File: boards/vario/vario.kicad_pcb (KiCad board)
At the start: 2 copper layers, 90 x 100 mm, 121 parts, among them J1 Conn_02x20_Odd_Even, J2 SD_Card, J3 Mini-DIN-6, Q1 2N7002, Q2 2N7002, Q3 2N7002, Q4 2N7002, Q5 2N7002, U1 74HC273PW, U10 74HC161PW, U11 MC74HC244ADT, U12 74HC74PW, U13 74HC74PW, U14 74HC08PW, U15 74HC74PW, U16 74HC74PW, U17 74HC161PW, U18 74HC273PW, U19 CD74HC280MT, U2 74HC161PW, U20 MC74HC151ADTR2G, U21 MC74HC151ADTR2G, U22 MC74HC244ADT, U23 CD74HC280MT, U24 SN74LV10APW, U25 74HC08PW, U26 74HC04PW, U27 74HC30D, U28 SN74HC32PWR, U29 SN74HC32PWR, U3 74HC74PW, U30 SN74HC32PWR, U31 SN74LV14APW, U32 SN74HC32PWR, U33 74HC08PW, U34 74HC273PW, U35 MC74HC244ADT, U36 IFX54441EJV33, U37 SN74HC139PW, U38 SN74HC32PWR, U4 74HC273PW, U5 MC74HC151ADTR2G, U6 MC74HC244ADT, U7 SN74LV14APW, U8 74HC273PW, U9 74HC273PW

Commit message: Vario: power nets
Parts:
- moved R5 214.2 mm to (129.5, 83.2), turned to 90 degrees
- moved C29 203.4 mm to (139.2, 70.0), turned to 180 degrees
- moved C33 201.7 mm to (132.8, 81.2), turned to 90 degrees
- moved Q2 200.9 mm to (130.5, 92.0)
- moved C34 200.8 mm to (138.8, 82.2), turned to 180 degrees
- moved C31 195.5 mm to (152.5, 73.2)
- moved U32 195.4 mm to (135.8, 63.5)
- moved D2 194.8 mm to (142.8, 52.5), turned to 180 degrees
- moved C36 194.3 mm to (152.5, 59.0)
- moved U33 191.4 mm to (149.0, 63.0)
- moved R19 191.3 mm to (146.4, 52.5), turned to 180 degrees
- moved C35 189.5 mm to (139.2, 59.5), turned to 180 degrees
- moved U3 188.5 mm to (135.8, 74.0)
- moved U31 188.4 mm to (135.5, 86.2)
- moved C28 185.8 mm to (153.8, 83.2)
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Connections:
- U1 pad 12: /SPI/reg_send_q4 -> /SPI/reg_send_q0
- U1 pad 13: /d4 -> /d0
- U1 pad 14: /d5 -> /d1
- U1 pad 15: /SPI/reg_send_q5 -> /SPI/reg_send_q1
- U1 pad 16: /SPI/reg_send_q6 -> /SPI/reg_send_q2
- U1 pad 17: /d6 -> /d2
- U1 pad 18: /d7 -> /d3
- U1 pad 19: /SPI/reg_send_q7 -> /SPI/reg_send_q3
- U1 pad 2: /SPI/reg_send_q0 -> /SPI/reg_send_q4
- U1 pad 3: /d0 -> /d4
- U1 pad 4: /d1 -> /d5
- U1 pad 5: /SPI/reg_send_q1 -> /SPI/reg_send_q5
- U1 pad 6: /SPI/reg_send_q2 -> /SPI/reg_send_q6
- U1 pad 7: /d2 -> /d6
- U1 pad 8: /d3 -> /d7
- U1 pad 9: /SPI/reg_send_q3 -> /SPI/reg_send_q7
- U13 pad 11: /ps2/send_clk_ena_clk -> /ps2/send_req
- U13 pad 13: /ps2/~send_rst -> /ps2/~send_clk_out_rst
- U13 pad 8: /ps2/~send_clk_ena -> /ps2/send_clk_out
- U13 pad 9: (no net) -> /ps2/~send_clk_out
- U15 pad 1: /ps2/~send_clk_out_rst -> /ps2/~send_rst
- U15 pad 3: /ps2/send_req -> /ps2/send_clk_ena_clk
- U15 pad 5: /ps2/~send_clk_out -> (no net)
- U15 pad 6: /ps2/send_clk_out -> /ps2/~send_clk_ena
- U18 pad 12: /ps2/send_data5 -> /ps2/send_data1
- U18 pad 13: /d4 -> /d0
- U18 pad 14: /d5 -> /d1
- U18 pad 15: /ps2/send_data6 -> /ps2/send_data2
- U18 pad 16: /ps2/send_data7 -> /ps2/send_data3
- U18 pad 17: /d6 -> /d2
- U18 pad 18: /d7 -> /d3
- U18 pad 19: /ps2/send_data8 -> /ps2/send_data4
- U18 pad 2: /ps2/send_data1 -> /ps2/send_data5
- U18 pad 3: /d0 -> /d4
- U18 pad 4: /d1 -> /d5
- U18 pad 5: /ps2/send_data2 -> /ps2/send_data6
- U18 pad 6: /ps2/send_data3 -> /ps2/send_data7
- U18 pad 7: /d2 -> /d6
- U18 pad 8: /d3 -> /d7
- U18 pad 9: /ps2/send_data4 -> /ps2/send_data8
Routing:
- net GND: track 0.00 -> 1167.6 mm, vias 0 -> 90
- net VCC: track 0.00 -> 609.3 mm, vias 0 -> 45
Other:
- rule trace_min: 0.2 -> 0.1524

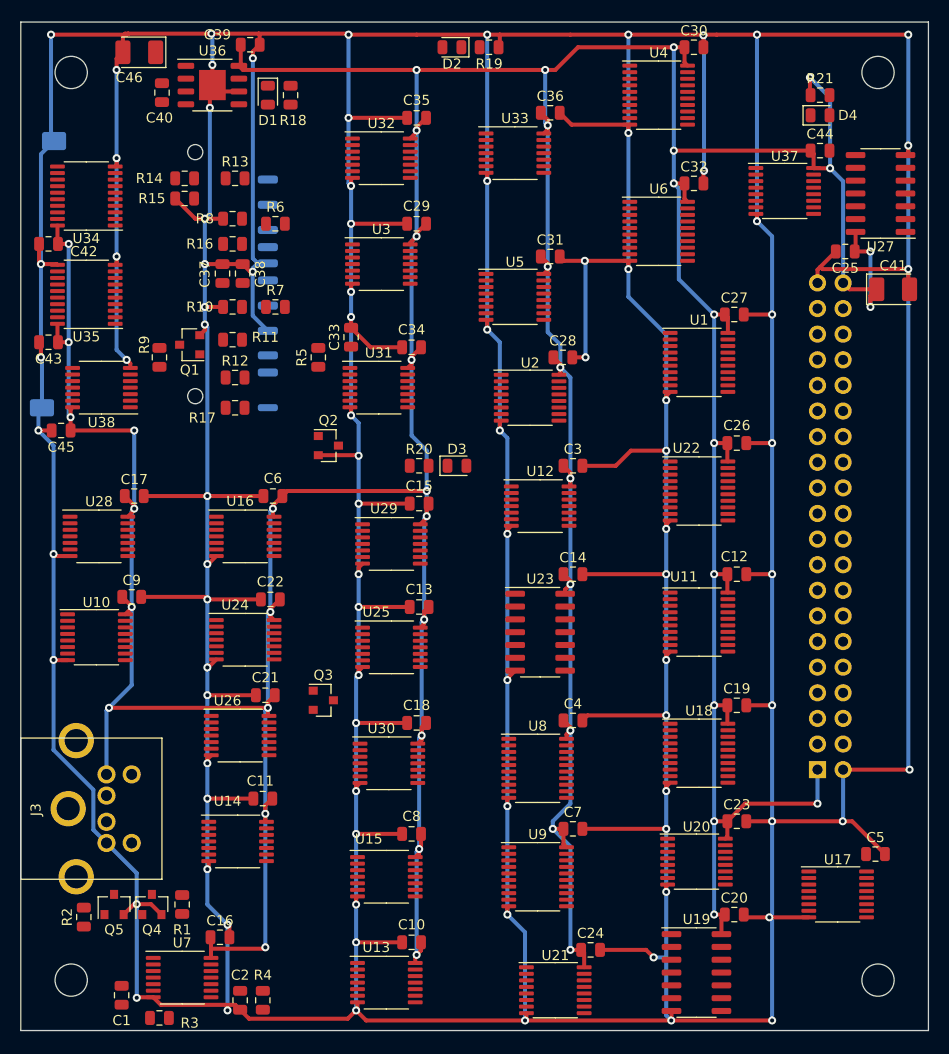
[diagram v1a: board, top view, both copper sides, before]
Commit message: Vario: board, delete redundant 7474
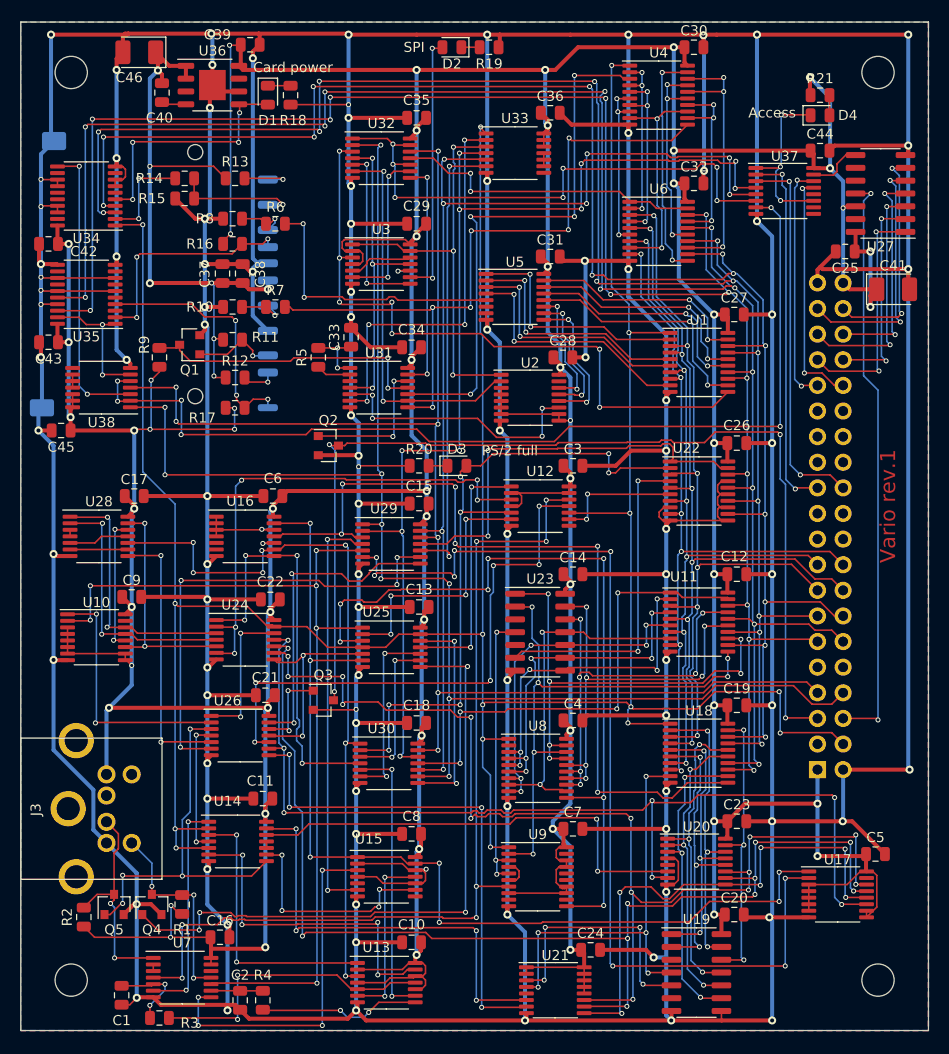
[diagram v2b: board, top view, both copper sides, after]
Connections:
- U16 pad 1: /ps2/~send_rst -> VCC
- U16 pad 3: /ps2/send_ena_clk -> VCC
- U16 pad 5: /ps2/~send_rdy -> (no net)
- U26 pad 13: rdy -> /ps2/rdy_out
- U28 pad 10: /ps2/~send_rdy -> /ps2/send_ena
- U29 pad 8: rdy -> /ps2/rdy_out
- U37 pad 13: /a8 -> /a9
- U37 pad 14: /a9 -> /a8
- U37 pad 2: /a1 -> /a0
- U37 pad 3: /a0 -> /a1
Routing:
- net ~rst: track 0.00 -> 306.2 mm, vias 0 -> 16
- net VCC: track 609.3 -> 811.3 mm, vias 45 -> 61
- net /d1: track 0.00 -> 186.4 mm, vias 0 -> 12
- net /d0: track 0.00 -> 181.4 mm, vias 0 -> 13
- net /d3: track 0.00 -> 171.4 mm, vias 0 -> 13
- net /d2: track 0.00 -> 171.2 mm, vias 0 -> 13
- net /~we: track 0.00 -> 149.8 mm, vias 0 -> 9
- net /~oe: track 0.00 -> 138.7 mm, vias 0 -> 7
- net /ps2/send_cnt1: track 0.00 -> 115.2 mm, vias 0 -> 10
- net /ps2/send_cnt0: track 0.00 -> 111.6 mm, vias 0 -> 14
- net /~ps2_data_sel: track 0.00 -> 111.2 mm, vias 0 -> 10
- net /~ps2_status_sel: track 0.00 -> 109.4 mm, vias 0 -> 8
- net rdy: track 0.00 -> 102.9 mm, vias 0 -> 4
- net /ps2/~send_rst: track 0.00 -> 101.3 mm, vias 0 -> 7
- net /ps2/send_cnt3: track 0.00 -> 99.1 mm, vias 0 -> 7
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- added copper zone on B.Cu, net GND
- added copper zone on F.Cu, net GND
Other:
- board text added: "Access"
- board text added: "Card power"
- board text added: "PS/2 full"
- board text added: "SPI"
- board text added: "Vario rev.1"

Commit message: Vario: add license notice
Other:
- board text added: "Licensed under the TAPR Open Hardware License (www.tapr.org/OHL)"
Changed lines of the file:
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@@
   (general
     (thickness 1.6)
-    (drawings 9)
+    (drawings 10)
     (tracks 3545)
     (zones 0)
@@
     )
   )
+  (gr_text "Licensed under the TAPR Open Hardware License\n(www.tapr.org/OHL)" (at 174.7 100.5 90) (layer B.SilkS)
+    (effects (font (size 1 1) (thickness 0.15)) (justify mirror))
+  )
   (gr_text SPI (at 139 52.5) (layer F.SilkS)
